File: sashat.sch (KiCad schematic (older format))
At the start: 0 parts

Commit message: Place HMC358 on schematic
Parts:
- added U1: HMC358, symbol HMC358
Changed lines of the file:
@@
 EESchema Schematic File Version 2
-LIBS:power
+LIBS:hittite
+LIBS:sashat-cache
 EELAYER 25 0
 EELAYER END
@@
 Comment4 ""
 $EndDescr
+$Comp
+L HMC358 U1
+U 1 1 553731C3
+P 3800 2700
+F 0 "U1" H 3600 3000 60  0000 C CNN
+F 1 "HMC358" H 3750 2400 60  0000 C CNN
+F 2 "" H 3700 3000 60  0000 C CNN
+F 3 "" H 3700 3000 60  0000 C CNN
+	1    3800 2700
+	1    0    0    -1
+$EndComp
 $EndSCHEMATC

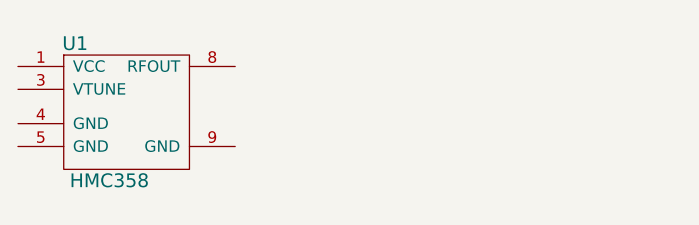
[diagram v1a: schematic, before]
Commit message: Add HMC526LC4 schematic part
It was also placed in the schematic and linked to the footprint
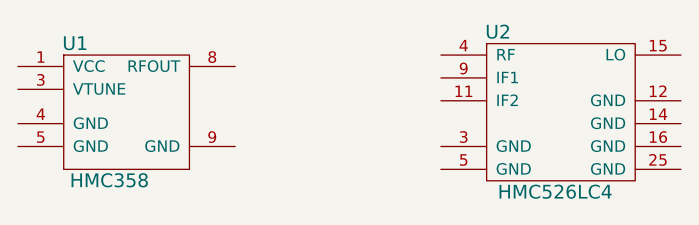
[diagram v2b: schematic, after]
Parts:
- added U2: HMC526LC4, hittite:LC4, symbol HMC526LC4
- U1: footprint (none) -> hittite:Hittite_MSOP8
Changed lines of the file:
@@
 F 0 "U1" H 3600 3000 60  0000 C CNN
 F 1 "HMC358" H 3750 2400 60  0000 C CNN
-F 2 "" H 3700 3000 60  0000 C CNN
+F 2 "hittite:Hittite_MSOP8" H 3700 3000 60  0001 C CNN
 F 3 "" H 3700 3000 60  0000 C CNN
 	1    3800 2700
 	1    0    0    -1
 $EndComp
+$Comp
+L HMC526LC4 U2
+U 1 1 5539B8CA
+P 5650 2500
+F 0 "U2" H 5450 2650 60  0000 C CNN
+F 1 "HMC526LC4" H 5700 1950 60  0000 C CNN
+F 2 "hittite:LC4" H 5650 2500 60  0001 C CNN
+F 3 "" H 5650 2500 60  0000 C CNN
+	1    5650 2500
+	1    0    0    -1
+$EndComp
